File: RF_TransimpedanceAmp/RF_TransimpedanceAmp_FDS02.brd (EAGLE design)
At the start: 76.2 x 38.1 mm, 39 parts, among them IC1 LT1964-5, IC2 OPA847, IC3 PMA-5452, IC4 ADM7150ARDZ-3.0, IC5 ADM7150ARDZ-5.0, X1 SMAJ502

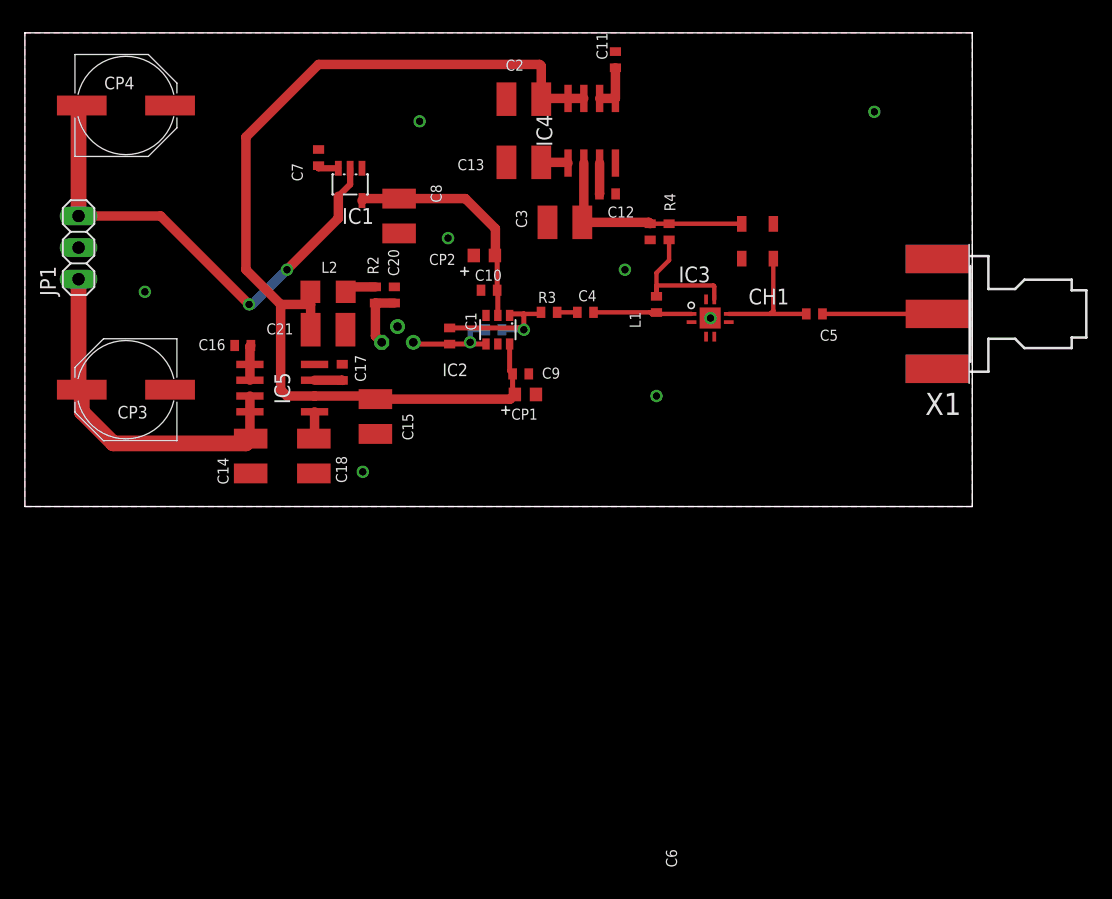
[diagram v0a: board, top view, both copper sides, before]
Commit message: Removed OPA847, using low-noise amplifiers with 50 ohm input as transimpedance gain.
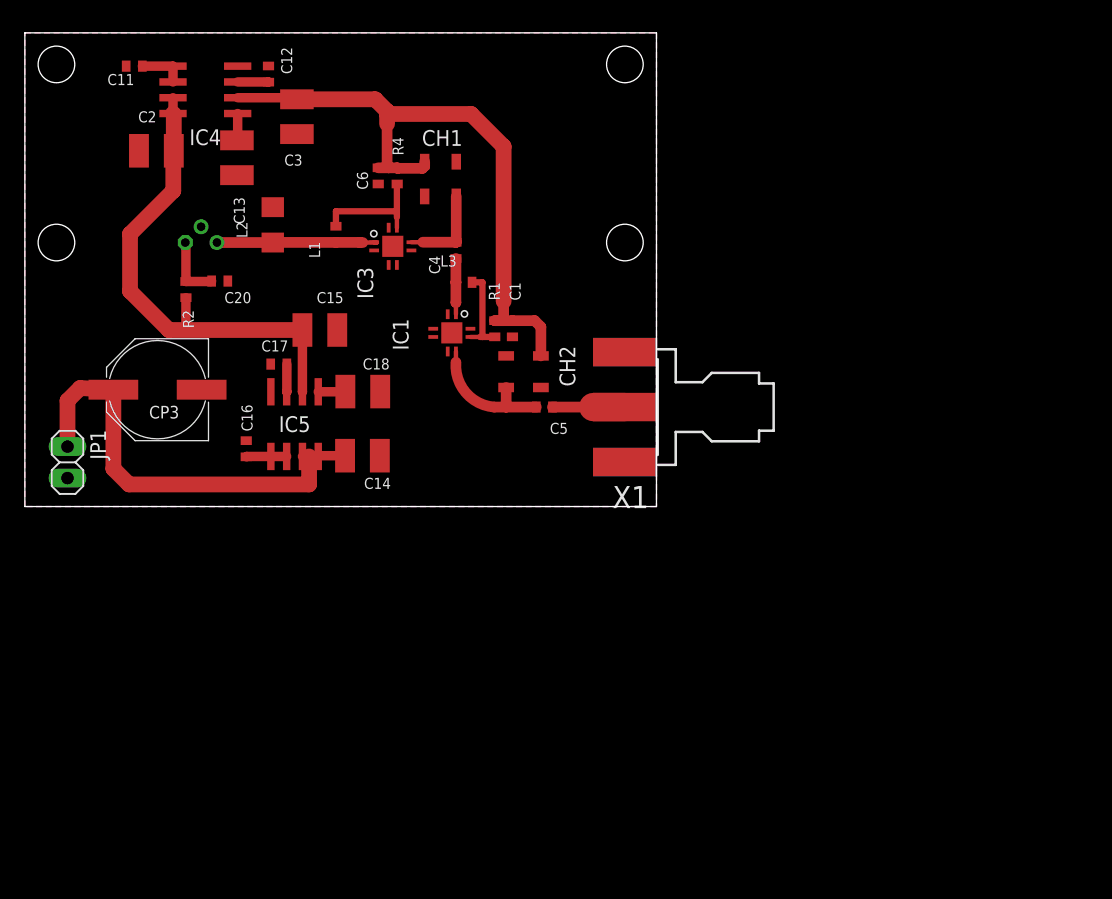
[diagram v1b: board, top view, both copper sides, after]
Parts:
- removed C10, C9: 100nF, rlc-jqi:0402
- removed C21, C8: 10uF, rlc-jqi:1210
- removed C7: 10nF, rlc-jqi:0402
- removed CP1, CP2: 6.8uF, rlc-jqi:0603P
- removed CP4: (no value), rlc-jqi:PANASONIC_F
- removed IC2: OPA847, opamp-jqi:SOT23-6
- removed R3: 50R, rlc-jqi:0402
- added CH2: TCCH-80, rf-jqi:GU1604
- added L3: 390nH, rlc-jqi:0402
- C1: value 6.2pF -> 100nF
- IC1: value LT1964-5 -> PMA-5452; device regulator-jqi:SOT23-5L -> rf-jqi:DQ849
- JP1: device pinhead:1X03 -> pinhead:1X02
- R1: value 10R -> 1k
- moved C11 38.7 mm to (8.80, 35.4), turned to 180 degrees
- moved IC4 32.0 mm to (14.5, 34.2), turned to 180 degrees
- moved C2 29.8 mm to (10.6, 28.6)
- moved C12 28.9 mm to (19.6, 34.8), turned to 90 degrees
- moved L1 26.4 mm to (25.0, 21.9)
- moved X1 26.2 mm to (49.5, 9.27)
- moved IC3 26.2 mm to (29.6, 20.0)
- moved CH1 26.0 mm to (33.4, 26.3)
- moved C3 23.2 mm to (21.9, 31.4), turned to 270 degrees
- moved C13 23.1 mm to (17.1, 28.1), turned to 270 degrees
- moved C5 23.0 mm to (41.8, 8.00)
- moved C6 22.3 mm to (28.4, 26.6)
- moved R4 22.3 mm to (29.9, 26.6)
- moved PD1 17.7 mm to (14.2, 21.2)
- moved JP1 17.3 mm to (3.43, 3.56), turned to 270 degrees
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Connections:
- removed net -15V: CP4.-, IC1.2, IC1.4, JP1.3
- removed net -5V: C10.2, C8.1, CP2.2, IC1.5, IC2.2
- removed net N$10: C7.1, IC1.3
- removed net N$4: C4.2, R3.2
- removed net N$5 (its old number): L2.1, R2.2
- new net RFPD1: C4.1, IC1.P$1, L3.1
- net +3V: now also C1.1, CH2.P$3, R1.2
- net +5V: now also R2.2; no longer C21.2, C9.2, CP1.1, IC2.6, L2.2
- net GND: now also C1.2, IC1.P$GND, L2.1; no longer C10.1, C21.1, C7.2, C8.2, C9.1, CP1.2, CP2.1, CP4.+, IC1.1, IC2.3
- net N$2: now also C5.2, CH2.P$1, IC1.P$6; no longer C1.2, IC2.4, PD1.P$3, R1.1
- net N$3: now also IC1.P$7, L3.2, R1.1; no longer C1.1, IC2.1, R1.2, R3.1
- net N$6: now also C4.2; no longer C5.2
- net RFPD: now also L2.2, PD1.P$3; no longer C4.1
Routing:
- net +5V: track 82.8 -> 41.2 mm
- net -15V: track 40.5 -> 0.00 mm, vias 2 -> 0
- net +3V: track 17.7 -> 52.7 mm
- net -5V: track 18.9 -> 0.00 mm
- net +15V: track 29.0 -> 36.2 mm
- net RFPD: track 8.45 -> 13.1 mm
- net RFPD1: track 0.00 -> 4.48 mm
- net N$3: track 11.7 -> 7.19 mm, vias 1 -> 0
- net N$6: track 10.8 -> 7.29 mm
- net N$7: track 9.23 -> 5.80 mm
- net N$5 (its old number): track 2.78 -> 0.00 mm
- net N$2: track 8.40 -> 10.6 mm, vias 1 -> 0
- net N$9: track 11.6 -> 9.65 mm
- net N$10: track 1.80 -> 0.00 mm
- net N$4: track 1.62 -> 0.00 mm
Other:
- board size 76.2 x 38.1 mm -> 50.8 x 38.1 mm
- board text added: "34 mil 50ohm trace"
